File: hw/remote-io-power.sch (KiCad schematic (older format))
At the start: 12 parts, among them Q1 DMG2305UX, Q2 DMMT5401, U1 AP1506

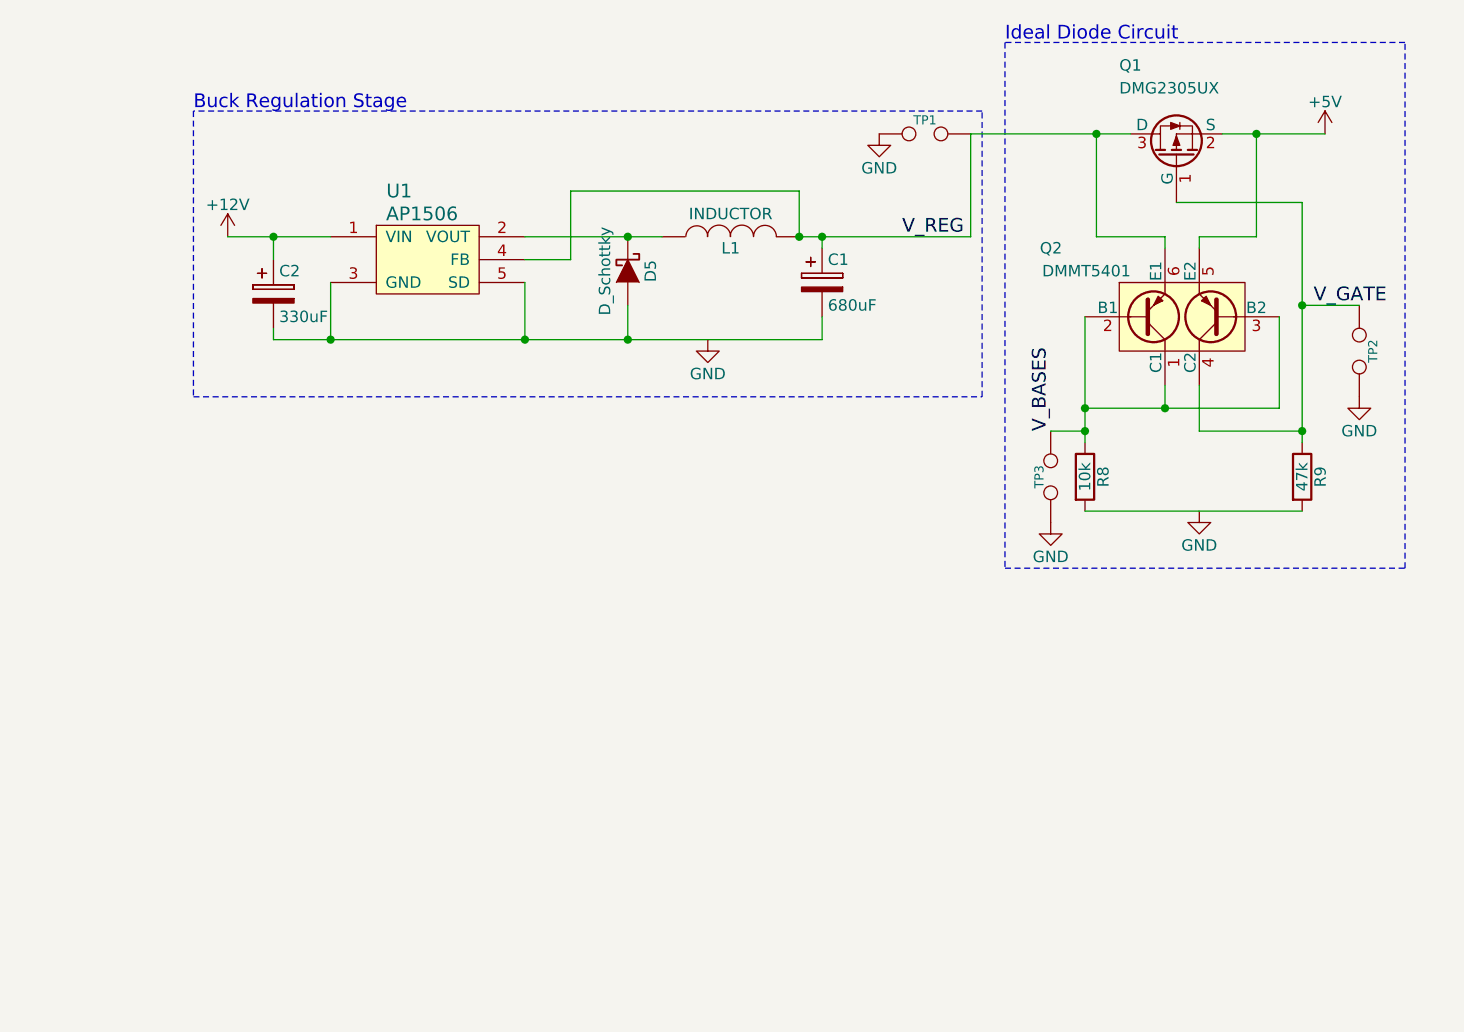
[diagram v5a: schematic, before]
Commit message: added CAN power, controller, and transceiver to schem and updated PCB
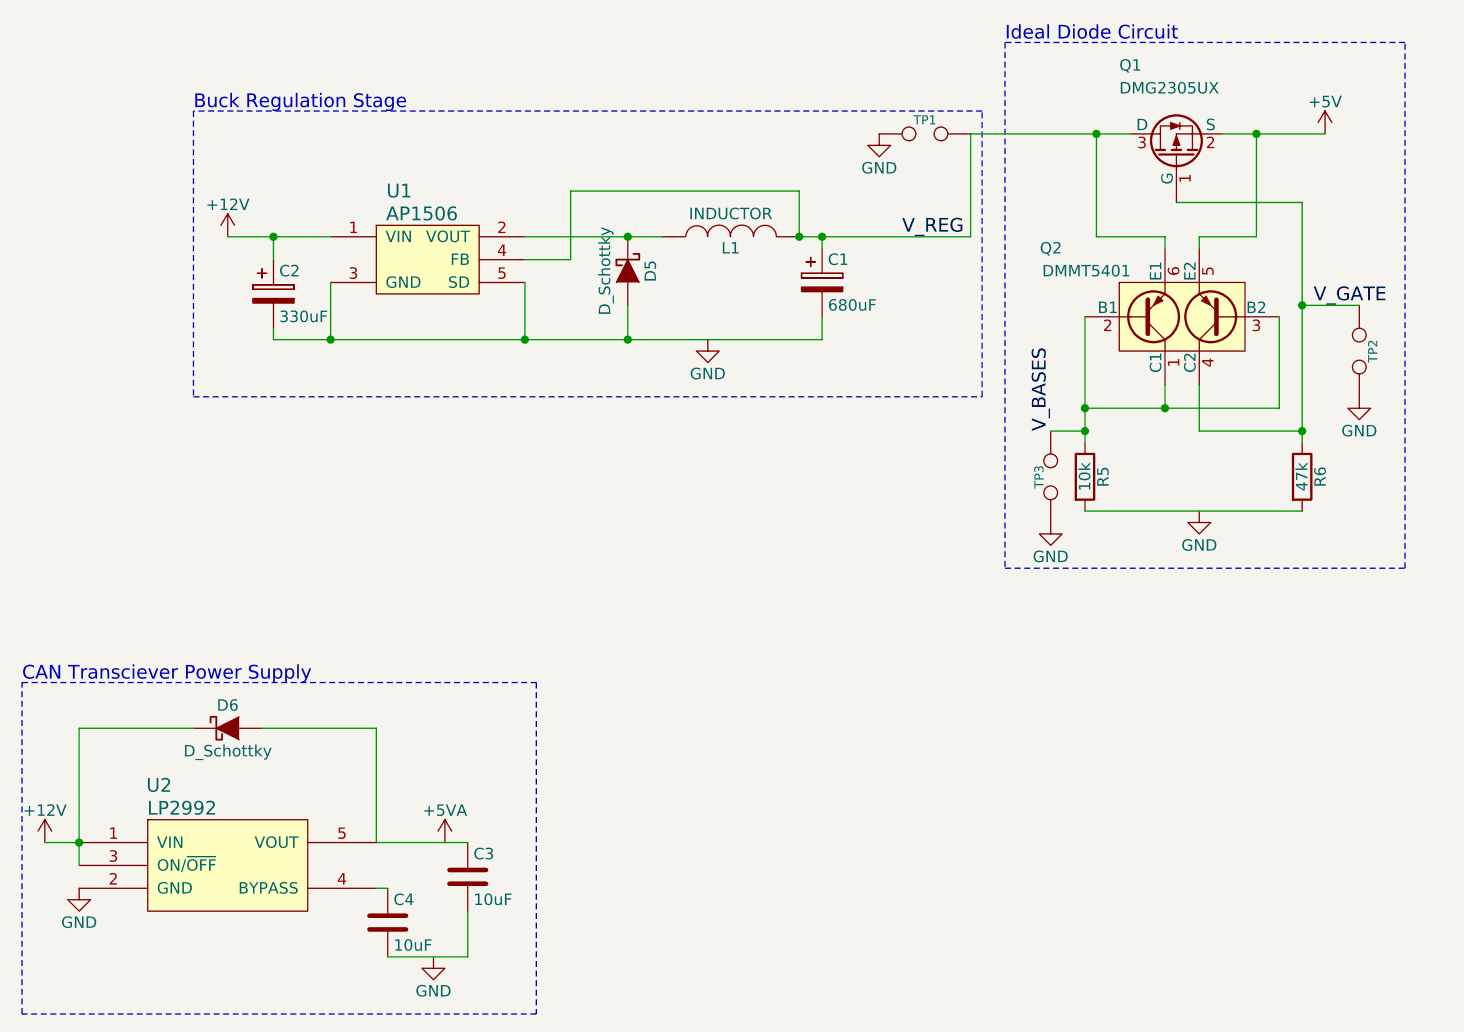
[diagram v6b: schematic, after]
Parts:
- added C3, C4: 10uF, Capacitors_SMD:C_0805_HandSoldering, symbol C
- added D6: D_Schottky, Diodes_SMD:Diode-SMB_Handsoldering, symbol D_Schottky
- added U2: LP2992, Housings_SOT-23_SOT-143_TSOT-6:SOT-23-5, symbol LP2992
- renumbered R8 to R5, R9 to R6
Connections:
- net +12V: now also D6.1 (K), U2.1 (VIN), U2.3 (ON/~OFF)
- net GND: now also U2.2 (GND)
- net at U1.3 (TAB): now also C1.2, C2.2, D5.2 (A), U1.5 (SD)
- new net: C4.1, U2.4 (BYPASS)
- new net: C3.1, D6.2 (A), U2.5 (VOUT)
- new net: C3.2, C4.2
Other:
- note added: "CAN Transciever Power Supply"
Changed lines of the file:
@@
 $Descr USLetter 11000 8500
 encoding utf-8
-Sheet 2 5
+Sheet 2 6
 Title "Remote I/O Power Section"
 Date "2015-06-15"
@@
 Connection ~ 6700 4200
 $Comp
-L R R8
+L R R5
 U 1 1 557F07EA
 P 6700 4500
-F 0 "R8" V 6780 4500 50  0000 C CNN
+F 0 "R5" V 6780 4500 50  0000 C CNN
 F 1 "10k" V 6700 4500 50  0000 C CNN
 F 2 "Resistors_SMD:R_0805_HandSoldering" V 6630 4500 30  0001 C CNN
@@
 $EndComp
 $Comp
-L R R9
+L R R6
 U 1 1 557F08A4
 P 7650 4500
-F 0 "R9" V 7730 4500 50  0000 C CNN
+F 0 "R6" V 7730 4500 50  0000 C CNN
 F 1 "47k" V 7650 4500 50  0000 C CNN
 F 2 "Resistors_SMD:R_0805_HandSoldering" V 7580 4500 30  0001 C CNN
@@
 Ideal Diode Circuit
 $Comp
-L +12V #PWR026
+L +12V #PWR028
 U 1 1 557F7629
 P 2950 3450
-F 0 "#PWR026" H 2950 3300 50  0001 C CNN
+F 0 "#PWR028" H 2950 3300 50  0001 C CNN
 F 1 "+12V" H 2950 3590 50  0000 C CNN
 F 2 "" H 2950 3450 60  0000 C CNN
@@
 $EndComp
 $Comp
-L +5V #PWR027
+L +5V #PWR029
 U 1 1 557F764F
 P 7750 3000
-F 0 "#PWR027" H 7750 2850 50  0001 C CNN
+F 0 "#PWR029" H 7750 2850 50  0001 C CNN
 F 1 "+5V" H 7750 3140 50  0000 C CNN
 F 2 "" H 7750 3000 60  0000 C CNN
@@
 V_GATE
 $Comp
-L GND #PWR028
+L GND #PWR030
 U 1 1 5582FAEC
 P 5050 3900
-F 0 "#PWR028" H 5050 3650 50  0001 C CNN
+F 0 "#PWR030" H 5050 3650 50  0001 C CNN
 F 1 "GND" H 5050 3750 50  0000 C CNN
 F 2 "" H 5050 3900 60  0000 C CNN
@@
 $EndComp
 $Comp
-L GND #PWR029
+L GND #PWR031
 U 1 1 5582FB3E
 P 6550 4700
-F 0 "#PWR029" H 6550 4450 50  0001 C CNN
+F 0 "#PWR031" H 6550 4450 50  0001 C CNN
 F 1 "GND" H 6550 4550 50  0000 C CNN
 F 2 "" H 6550 4700 60  0000 C CNN
@@
 $EndComp
 $Comp
-L GND #PWR030
+L GND #PWR032
 U 1 1 5582FB61
 P 7200 4650
-F 0 "#PWR030" H 7200 4400 50  0001 C CNN
+F 0 "#PWR032" H 7200 4400 50  0001 C CNN
 F 1 "GND" H 7200 4500 50  0000 C CNN
 F 2 "" H 7200 4650 60  0000 C CNN
@@
 $EndComp
 $Comp
-L GND #PWR031
+L GND #PWR033
 U 1 1 5582FB89
 P 5800 3000
-F 0 "#PWR031" H 5800 2750 50  0001 C CNN
+F 0 "#PWR033" H 5800 2750 50  0001 C CNN
 F 1 "GND" H 5800 2850 50  0000 C CNN
 F 2 "" H 5800 3000 60  0000 C CNN
@@
 $EndComp
 $Comp
-L GND #PWR032
+L GND #PWR034
 U 1 1 5582FBB1
 P 7900 4150
-F 0 "#PWR032" H 7900 3900 50  0001 C CNN
+F 0 "#PWR034" H 7900 3900 50  0001 C CNN
 F 1 "GND" H 7900 4000 50  0000 C CNN
 F 2 "" H 7900 4150 60  0000 C CNN
@@
 	1    0    0    -1
 $EndComp
+$Comp
+L LP2992 U2
+U 1 1 5584C1F6
+P 2950 6200
+F 0 "U2" H 2650 6550 60  0000 C CNN
+F 1 "LP2992" H 2750 6450 60  0000 C CNN
+F 2 "Housings_SOT-23_SOT-143_TSOT-6:SOT-23-5" H 2950 6400 60  0001 C CNN
+F 3 "" H 2950 6400 60  0000 C CNN
+	1    2950 6200
+	1    0    0    -1
+$EndComp
+$Comp
+L C C4
+U 1 1 5584C1FD
+P 3650 6450
+F 0 "C4" H 3675 6550 50  0000 L CNN
+F 1 "10uF" H 3675 6350 50  0000 L CNN
+F 2 "Capacitors_SMD:C_0805_HandSoldering" H 3688 6300 30  0001 C CNN
+F 3 "" H 3650 6450 60  0000 C CNN
+	1    3650 6450
+	1    0    0    -1
+$EndComp
+$Comp
+L GND #PWR035
+U 1 1 5584C204
+P 3850 6600
+F 0 "#PWR035" H 3850 6350 50  0001 C CNN
+F 1 "GND" H 3850 6450 50  0000 C CNN
+F 2 "" H 3850 6600 60  0000 C CNN
+F 3 "" H 3850 6600 60  0000 C CNN
+	1    3850 6600
+	1    0    0    -1
+$EndComp
+Wire Wire Line
+	3600 6300 3650 6300
+$Comp
+L C C3
+U 1 1 5584C20B
+P 4000 6250
+F 0 "C3" H 4025 6350 50  0000 L CNN
+F 1 "10uF" H 4025 6150 50  0000 L CNN
+F 2 "Capacitors_SMD:C_0805_HandSoldering" H 4038 6100 30  0001 C CNN
+F 3 "" H 4000 6250 60  0000 C CNN
+	1    4000 6250
+	1    0    0    -1
+$EndComp
+Wire Wire Line
+	3600 6100 4000 6100
+Wire Wire Line
+	3650 6600 4000 6600
+Wire Wire Line
+	4000 6600 4000 6400
+$Comp
+L D_Schottky D6
+U 1 1 5584C215
+P 2950 5600
+F 0 "D6" H 2950 5700 50  0000 C CNN
+F 1 "D_Schottky" H 2950 5500 50  0000 C CNN
+F 2 "Diodes_SMD:Diode-SMB_Handsoldering" H 2950 5600 60  0001 C CNN
+F 3 "" H 2950 5600 60  0000 C CNN
+	1    2950 5600
+	1    0    0    -1
+$EndComp
+Wire Wire Line
+	2300 5600 2300 6200
+Wire Wire Line
+	2300 5600 2800 5600
+Wire Wire Line
+	3100 5600 3600 5600
+Wire Wire Line
+	3600 5600 3600 6100
+Connection ~ 2300 6100
+$Comp
+L GND #PWR036
+U 1 1 5584C221
+P 2300 6300
+F 0 "#PWR036" H 2300 6050 50  0001 C CNN
+F 1 "GND" H 2300 6150 50  0000 C CNN
+F 2 "" H 2300 6300 60  0000 C CNN
+F 3 "" H 2300 6300 60  0000 C CNN
+	1    2300 6300
+	1    0    0    -1
+$EndComp
+$Comp
+L +5VA #PWR037
+U 1 1 5584C227
+P 3900 6100
+F 0 "#PWR037" H 3900 5950 50  0001 C CNN
+F 1 "+5VA" H 3900 6240 50  0000 C CNN
+F 2 "" H 3900 6100 60  0000 C CNN
+F 3 "" H 3900 6100 60  0000 C CNN
+	1    3900 6100
+	1    0    0    -1
+$EndComp
+Wire Notes Line
+	2050 5400 4300 5400
+Wire Notes Line
+	4300 5400 4300 6850
+Wire Notes Line
+	4300 6850 2050 6850
+Wire Notes Line
+	2050 6850 2050 5400
+Text Notes 2050 5400 0    60   ~ 0
+CAN Transciever Power Supply
+$Comp
+L +12V #PWR038
+U 1 1 55852018
+P 2150 6100
+F 0 "#PWR038" H 2150 5950 50  0001 C CNN
+F 1 "+12V" H 2150 6240 50  0000 C CNN
+F 2 "" H 2150 6100 60  0000 C CNN
+F 3 "" H 2150 6100 60  0000 C CNN
+	1    2150 6100
+	1    0    0    -1
+$EndComp
+Wire Wire Line
+	2150 6100 2300 6100
 $EndSCHEMATC

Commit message: Started fucking aroond with pcb layout. Power is tricky...
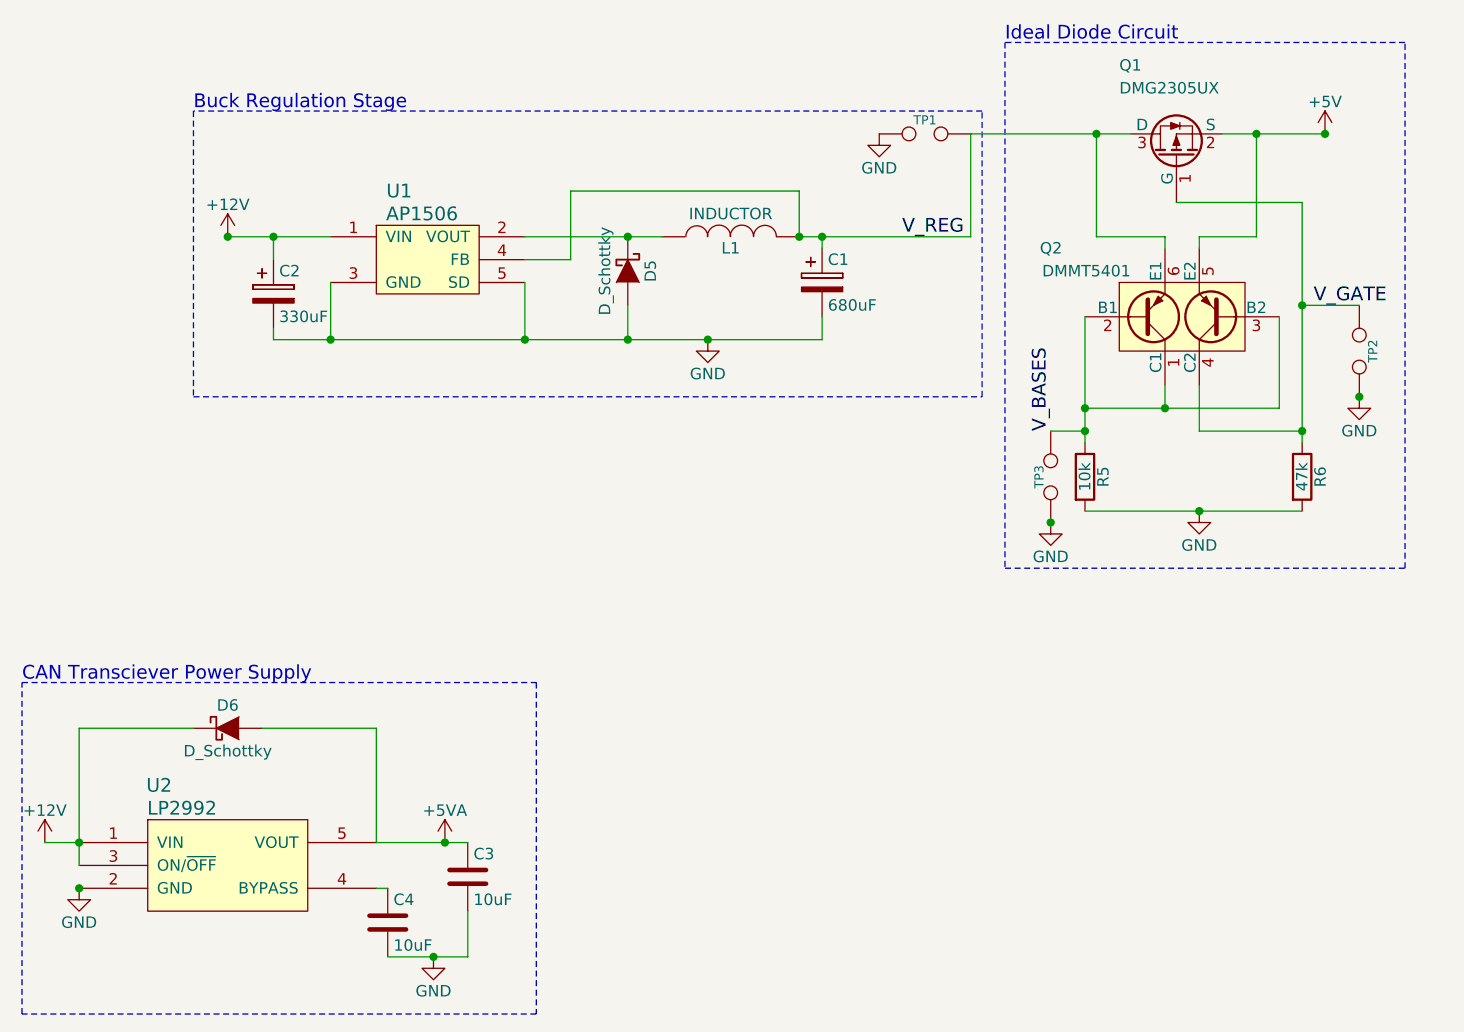
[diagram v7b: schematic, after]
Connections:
- net +5VA: now also C3.1, D6.2 (A), U2.5 (VOUT)
- net GND: now also C1.2, C2.2, C3.2, C4.2, D5.2 (A), R5.2, R6.2, U1.3 (TAB), U1.5 (SD)
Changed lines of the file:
@@
 Wire Wire Line
 	2150 6100 2300 6100
+Connection ~ 5050 3900
+Connection ~ 3850 6600
+Connection ~ 3900 6100
+Connection ~ 2300 6300
+Connection ~ 7200 4650
+Connection ~ 7750 3000
+Connection ~ 7900 4150
+Connection ~ 2950 3450
+Connection ~ 6550 4700
 $EndSCHEMATC

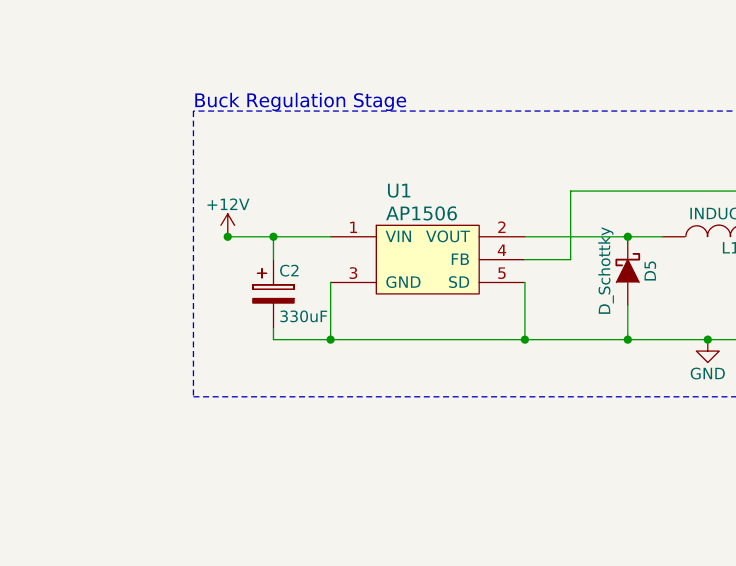
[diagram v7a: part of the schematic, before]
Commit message: All parts in hat-spec-size board
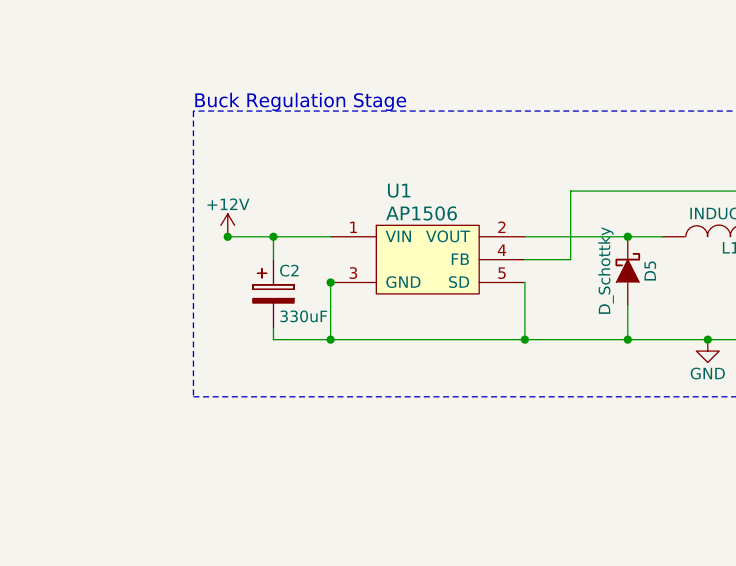
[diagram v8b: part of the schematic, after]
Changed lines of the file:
@@
 $Descr USLetter 11000 8500
 encoding utf-8
-Sheet 2 6
+Sheet 2 5
 Title "Remote I/O Power Section"
 Date "2015-06-15"
@@
 Ideal Diode Circuit
 $Comp
-L +12V #PWR028
+L +12V #PWR027
 U 1 1 557F7629
 P 2950 3450
-F 0 "#PWR028" H 2950 3300 50  0001 C CNN
+F 0 "#PWR027" H 2950 3300 50  0001 C CNN
 F 1 "+12V" H 2950 3590 50  0000 C CNN
 F 2 "" H 2950 3450 60  0000 C CNN
@@
 $EndComp
 $Comp
-L +5V #PWR029
+L +5V #PWR028
 U 1 1 557F764F
 P 7750 3000
-F 0 "#PWR029" H 7750 2850 50  0001 C CNN
+F 0 "#PWR028" H 7750 2850 50  0001 C CNN
 F 1 "+5V" H 7750 3140 50  0000 C CNN
 F 2 "" H 7750 3000 60  0000 C CNN
@@
 V_GATE
 $Comp
-L GND #PWR030
+L GND #PWR029
 U 1 1 5582FAEC
 P 5050 3900
-F 0 "#PWR030" H 5050 3650 50  0001 C CNN
+F 0 "#PWR029" H 5050 3650 50  0001 C CNN
 F 1 "GND" H 5050 3750 50  0000 C CNN
 F 2 "" H 5050 3900 60  0000 C CNN
@@
 $EndComp
 $Comp
-L GND #PWR031
+L GND #PWR030
 U 1 1 5582FB3E
 P 6550 4700
-F 0 "#PWR031" H 6550 4450 50  0001 C CNN
+F 0 "#PWR030" H 6550 4450 50  0001 C CNN
 F 1 "GND" H 6550 4550 50  0000 C CNN
 F 2 "" H 6550 4700 60  0000 C CNN
@@
 $EndComp
 $Comp
-L GND #PWR032
+L GND #PWR031
 U 1 1 5582FB61
 P 7200 4650
-F 0 "#PWR032" H 7200 4400 50  0001 C CNN
+F 0 "#PWR031" H 7200 4400 50  0001 C CNN
 F 1 "GND" H 7200 4500 50  0000 C CNN
 F 2 "" H 7200 4650 60  0000 C CNN
@@
 $EndComp
 $Comp
-L GND #PWR033
+L GND #PWR032
 U 1 1 5582FB89
 P 5800 3000
-F 0 "#PWR033" H 5800 2750 50  0001 C CNN
+F 0 "#PWR032" H 5800 2750 50  0001 C CNN
 F 1 "GND" H 5800 2850 50  0000 C CNN
 F 2 "" H 5800 3000 60  0000 C CNN
@@
 $EndComp
 $Comp
-L GND #PWR034
+L GND #PWR033
 U 1 1 5582FBB1
 P 7900 4150
-F 0 "#PWR034" H 7900 3900 50  0001 C CNN
+F 0 "#PWR033" H 7900 3900 50  0001 C CNN
 F 1 "GND" H 7900 4000 50  0000 C CNN
 F 2 "" H 7900 4150 60  0000 C CNN
@@
 $EndComp
 $Comp
-L GND #PWR035
+L GND #PWR034
 U 1 1 5584C204
 P 3850 6600
-F 0 "#PWR035" H 3850 6350 50  0001 C CNN
+F 0 "#PWR034" H 3850 6350 50  0001 C CNN
 F 1 "GND" H 3850 6450 50  0000 C CNN
 F 2 "" H 3850 6600 60  0000 C CNN
@@
 Connection ~ 2300 6100
 $Comp
-L GND #PWR036
+L GND #PWR035
 U 1 1 5584C221
 P 2300 6300
-F 0 "#PWR036" H 2300 6050 50  0001 C CNN
+F 0 "#PWR035" H 2300 6050 50  0001 C CNN
 F 1 "GND" H 2300 6150 50  0000 C CNN
 F 2 "" H 2300 6300 60  0000 C CNN
@@
 $EndComp
 $Comp
-L +5VA #PWR037
+L +5VA #PWR036
 U 1 1 5584C227
 P 3900 6100
-F 0 "#PWR037" H 3900 5950 50  0001 C CNN
+F 0 "#PWR036" H 3900 5950 50  0001 C CNN
 F 1 "+5VA" H 3900 6240 50  0000 C CNN
 F 2 "" H 3900 6100 60  0000 C CNN
@@
 CAN Transciever Power Supply
 $Comp
-L +12V #PWR038
+L +12V #PWR037
 U 1 1 55852018
 P 2150 6100
-F 0 "#PWR038" H 2150 5950 50  0001 C CNN
+F 0 "#PWR037" H 2150 5950 50  0001 C CNN
 F 1 "+12V" H 2150 6240 50  0000 C CNN
 F 2 "" H 2150 6100 60  0000 C CNN
@@
 Connection ~ 2950 3450
 Connection ~ 6550 4700
+Connection ~ 3400 3650
 $EndSCHEMATC
